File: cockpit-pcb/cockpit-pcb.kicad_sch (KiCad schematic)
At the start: 9 parts, among them J3 Button 1 Connector, J4 Button 2 Connector, J5 Button 3 Connector, J6 LED 1 Connector, J7 LED 2 Connector, J8 LED 3 Connector

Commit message: Board routing
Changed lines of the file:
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@@
 		)
 	)
-	(text_box "Button pins (A6, A7 and A8) must be configured in pull-down mode."
-		(exclude_from_sim no)
-		(at 72.39 59.69 0)
-		(size 36.195 5.715)
+	(text_box "Button pins (B13, B12 and B11) must be configured in pull-down mode."
+		(exclude_from_sim no)
+		(at 68.58 59.69 0)
+		(size 40.005 5.715)
 		(margins 0.9525 0.9525 0.9525 0.9525)
 		(stroke
@@
 			)
 		)
-		(pin "PA8" input
+		(pin "PB13" input
+			(at 45.72 16.51 0)
+			(effects
+				(font
+					(size 1.27 1.27)
+				)
+				(justify right)
+			)
+		)
+		(pin "PB12" input
+			(at 45.72 19.05 0)
+			(effects
+				(font
+					(size 1.27 1.27)
+				)
+				(justify right)
+			)
+		)
+		(pin "PA8" output
+			(at 45.72 27.94 0)
+			(effects
+				(font
+					(size 1.27 1.27)
+				)
+				(justify right)
+			)
+		)
+		(pin "PA7" output
+			(at 45.72 30.48 0)
+			(effects
+				(font
+					(size 1.27 1.27)
+				)
+				(justify right)
+			)
+		)
+		(pin "PA6" output
+			(at 45.72 33.02 0)
+			(effects
+				(font
+					(size 1.27 1.27)
+				)
+				(justify right)
+			)
+		)
+		(pin "PB11" input
 			(at 45.72 21.59 0)
 			(effects
 				(font
-					(size 1.27 1.27)
-				)
-				(justify right)
-			)
-		)
-		(pin "PB11" output
-			(at 45.72 27.94 0)
-			(effects
-				(font
-					(size 1.27 1.27)
-				)
-				(justify right)
-			)
-		)
-		(pin "PB12" output
-			(at 45.72 30.48 0)
-			(effects
-				(font
-					(size 1.27 1.27)
-				)
-				(justify right)
-			)
-		)
-		(pin "PB13" output
-			(at 45.72 33.02 0)
-			(effects
-				(font
-					(size 1.27 1.27)
-				)
-				(justify right)
-			)
-		)
-		(pin "PA6" input
-			(at 45.72 16.51 0)
-			(effects
-				(font
-					(size 1.27 1.27)
-				)
-				(justify right)
-			)
-		)
-		(pin "PA7" input
-			(at 45.72 19.05 0)
-			(effects
-				(font

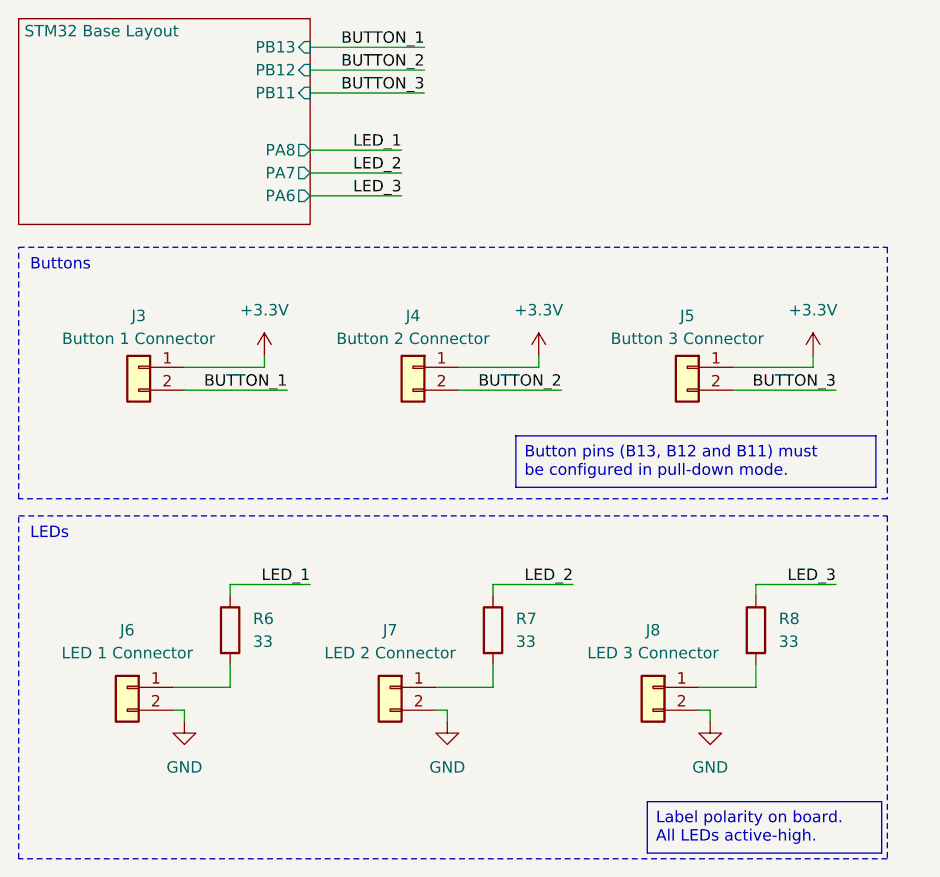
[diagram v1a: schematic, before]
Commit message: Increase LED resistors
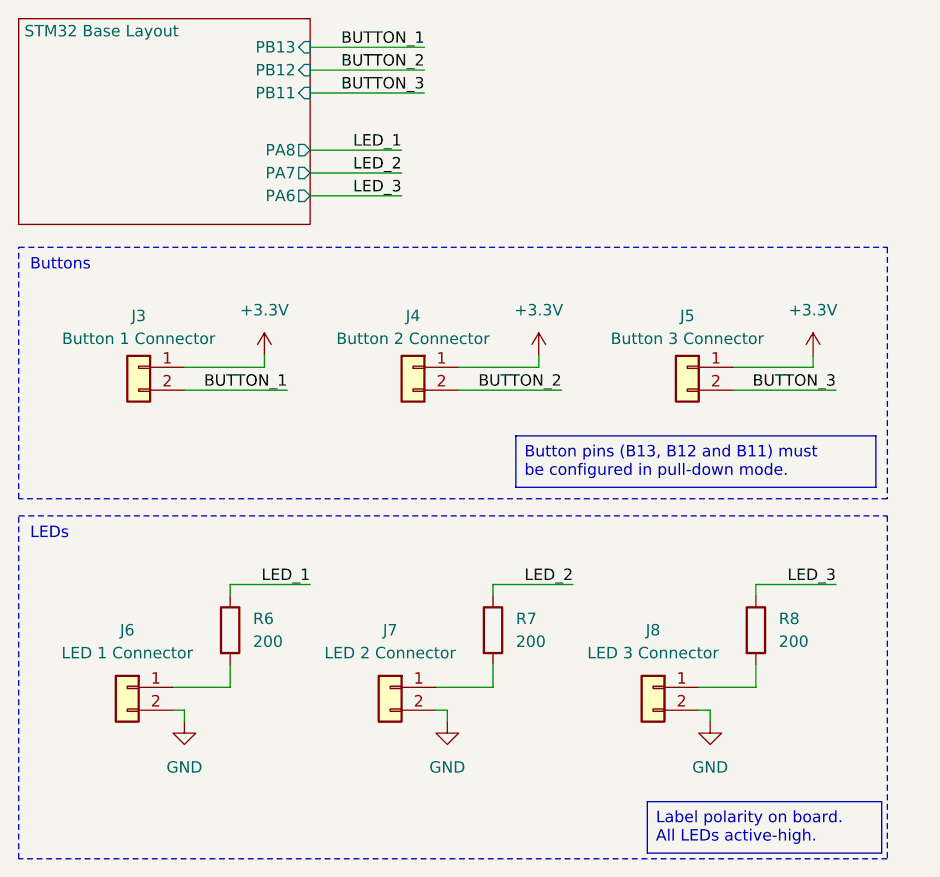
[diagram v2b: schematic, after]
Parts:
- R6, R7, R8: value 33 -> 200; JLCPCB C23140 -> C8218
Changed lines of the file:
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@@
 			)
 		)
-		(property "Value" "33"
+		(property "Value" "200"
 			(at 97.79 82.5499 0)
 			(effects
@@
 			)
 		)
-		(property "JLCPCB" "C23140"
+		(property "JLCPCB" "C8218"
 			(at 95.25 81.28 0)
 			(effects
@@
 			)
 		)
-		(property "Value" "33"
+		(property "Value" "200"
 			(at 39.37 82.5499 0)
 			(effects
@@
 			)
 		)
-		(property "JLCPCB" "C23140"
+		(property "JLCPCB" "C8218"
 			(at 36.83 81.28 0)
 			(effects
@@
 			)
 		)
-		(property "Value" "33"
+		(property "Value" "200"
 			(at 68.58 82.5499 0)
 			(effects
@@
 			)
 		)
-		(property "JLCPCB" "C23140"
+		(property "JLCPCB" "C8218"
 			(at 66.04 81.28 0)
 			(effects
